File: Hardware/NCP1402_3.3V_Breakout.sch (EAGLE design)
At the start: 12 parts, among them U1 NCP1402

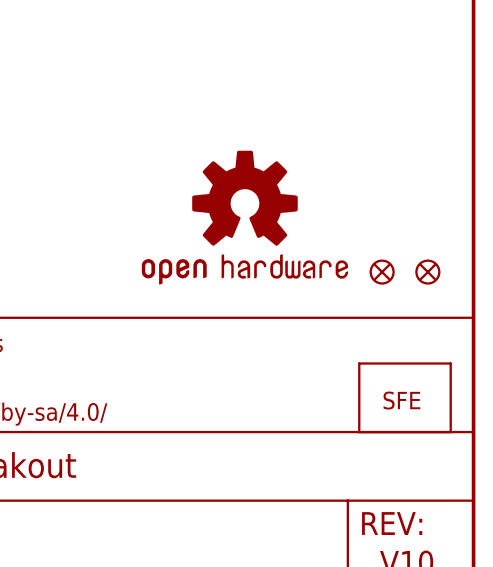
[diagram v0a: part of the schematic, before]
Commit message: changed micro fids to regular
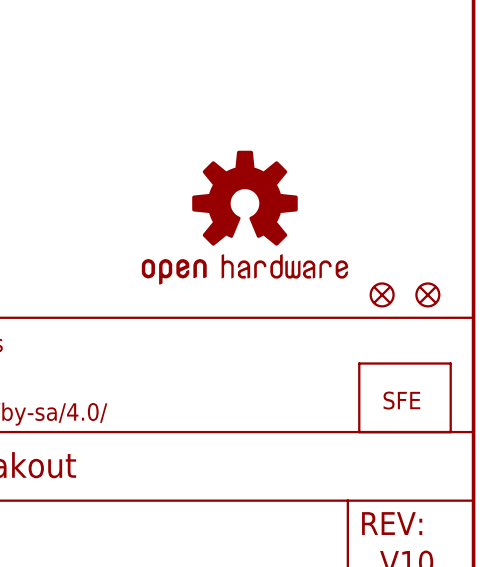
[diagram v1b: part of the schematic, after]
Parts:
- removed JP3, JP4: FIDUCIALUFIDUCIAL, SparkFun:FIDUCIALUFIDUCIAL
- added FID1, FID2: FIDUCIAL1X2, SparkFun-Aesthetics:FIDUCIAL1X2
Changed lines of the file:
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@@
 <?xml version="1.0" encoding="utf-8"?>
 <!DOCTYPE eagle SYSTEM "eagle.dtd">
-<eagle version="6.4">
+<eagle version="6.5.0">
 <drawing>
 <settings>
@@
 <part name="JP2" library="SparkFun" deviceset="LOGO-SFE" device="SK"/>
 <part name="U$1" library="SparkFun" deviceset="OSHW-LOGO" device="S"/>
-<part name="JP3" library="SparkFun" deviceset="FIDUCIAL" device="UFIDUCIAL"/>
-<part name="JP4" library="SparkFun" deviceset="FIDUCIAL" device="UFIDUCIAL"/>
 <part name="U$2" library="SparkFun" deviceset="CREATIVE_COMMONS" device=""/>
+<part name="FID1" library="SparkFun-Aesthetics" deviceset="FIDUCIAL" device="1X2"/>
+<part name="FID2" library="SparkFun-Aesthetics" deviceset="FIDUCIAL" device="1X2"/>
 </parts>
 <sheets>
@@
 <instance part="JP2" gate="G$1" x="238.76" y="25.4"/>
 <instance part="U$1" gate="G$1" x="223.52" y="48.26"/>
-<instance part="JP3" gate="G$1" x="243.84" y="40.64"/>
-<instance part="JP4" gate="G$1" x="238.76" y="40.64"/>
 <instance part="U$2" gate="G$1" x="7.62" y="7.62"/>
+<instance part="FID1" gate="G$1" x="238.76" y="38.1"/>
+<instance part="FID2" gate="G$1" x="243.84" y="38.1"/>
 </instances>
 <busses>
